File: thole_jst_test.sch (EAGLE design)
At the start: 3 parts, among them J1 Vertical Qwiic Connector

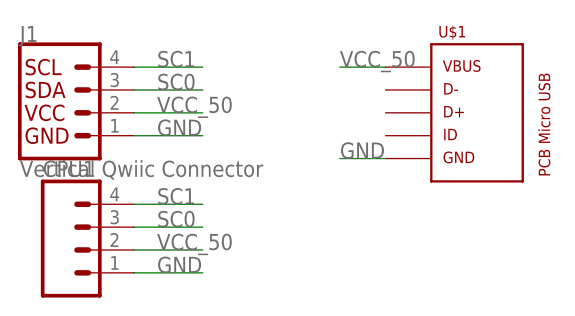
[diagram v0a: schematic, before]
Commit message: Goddamit jst throughole test wasn't throughhole
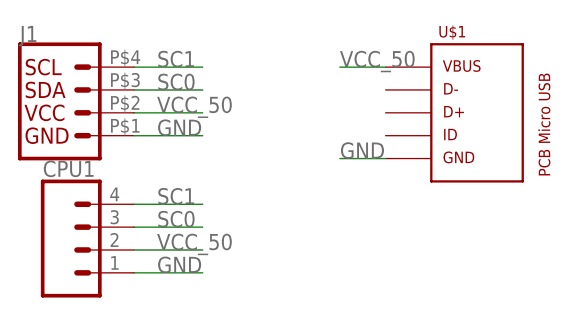
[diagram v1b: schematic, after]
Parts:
- J1: device SparkFun-Connectors:QWIIC_CONNECTOR -> 00jim:QWIIC_CONNECTORJST04_1MM_HOLE
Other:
- moved on the sheet: J1
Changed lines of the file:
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@@
 <grid distance="0.1" unitdist="inch" unit="inch" style="lines" multiple="1" display="no" altdistance="0.01" altunitdist="inch" altunit="inch"/>
 <layers>
-<layer number="1" name="Top" color="4" fill="1" visible="no" active="no"/>
-<layer number="16" name="Bottom" color="1" fill="1" visible="no" active="no"/>
-<layer number="17" name="Pads" color="2" fill="1" visible="no" active="no"/>
-<layer number="18" name="Vias" color="2" fill="1" visible="no" active="no"/>
-<layer number="19" name="Unrouted" color="6" fill="1" visible="no" active="no"/>
-<layer number="20" name="Dimension" color="24" fill="1" visible="no" active="no"/>
-<layer number="21" name="tPlace" color="7" fill="1" visible="no" active="no"/>
-<layer number="22" name="bPlace" color="7" fill="1" visible="no" active="no"/>
-<layer number="23" name="tOrigins" color="15" fill="1" visible="no" active="no"/>
-<layer number="24" name="bOrigins" color="15" fill="1" visible="no" active="no"/>
-<layer number="25" name="tNames" color="7" fill="1" visible="no" active="no"/>
-<layer number="26" name="bNames" color="7" fill="1" visible="no" active="no"/>
-<layer number="27" name="tValues" color="7" fill="1" visible="no" active="no"/>
-<layer number="28" name="bValues" color="7" fill="1" visible="no" active="no"/>
+<layer number="1" name="Top" color="4" fill="1" visible="yes" active="no"/>
+<layer number="16" name="Bottom" color="1" fill="1" visible="yes" active="no"/>
+<layer number="17" name="Pads" color="2" fill="1" visible="yes" active="no"/>
+<layer number="18" name="Vias" color="2" fill="1" visible="yes" active="no"/>
+<layer number="19" name="Unrouted" color="6" fill="1" visible="yes" active="no"/>
+<layer number="20" name="Dimension" color="24" fill="1" visible="yes" active="no"/>
+<layer number="21" name="tPlace" color="7" fill="1" visible="yes" active="no"/>
+<layer number="22" name="bPlace" color="7" fill="1" visible="yes" active="no"/>
+<layer number="23" name="tOrigins" color="15" fill="1" visible="yes" active="no"/>
+<layer number="24" name="bOrigins" color="15" fill="1" visible="yes" active="no"/>
+<layer number="25" name="tNames" color="7" fill="1" visible="yes" active="no"/>
+<layer number="26" name="bNames" color="7" fill="1" visible="yes" active="no"/>
+<layer number="27" name="tValues" color="7" fill="1" visible="yes" active="no"/>
+<layer number="28" name="bValues" color="7" fill="1" visible="yes" active="no"/>
 <layer number="29" name="tStop" color="7" fill="3" visible="no" active="no"/>
 <layer number="30" name="bStop" color="7" fill="6" visible="no" active="no"/>
@@
 <layer number="35" name="tGlue" color="7" fill="4" visible="no" active="no"/>
 <layer number="36" name="bGlue" color="7" fill="5" visible="no" active="no"/>
-<layer number="37" name="tTest" color="7" fill="1" visible="no" active="no"/>
-<layer number="38" name="bTest" color="7" fill="1" visible="no" active="no"/>
+<layer number="37" name="tTest" color="7" fill="1" visible="yes" active="no"/>
+<layer number="38" name="bTest" color="7" fill="1" visible="yes" active="no"/>
 <layer number="39" name="tKeepout" color="4" fill="11" visible="no" active="no"/>
 <layer number="40" name="bKeepout" color="1" fill="11" visible="no" active="no"/>
@@
 <layer number="44" name="Drills" color="7" fill="1" visible="no" active="no"/>
 <layer number="45" name="Holes" color="7" fill="1" visible="no" active="no"/>
-<layer number="46" name="Milling" color="3" fill="1" visible="no" active="no"/>
-<layer number="47" name="Measures" color="7" fill="1" visible="no" active="no"/>
-<layer number="48" name="Document" color="7" fill="1" visible="no" active="no"/>
-<layer number="49" name="Reference" color="7" fill="1" visible="no" active="no"/>
-<layer number="50" name="dxf" color="7" fill="1" visible="no" active="no"/>
-<layer number="51" name="tDocu" color="7" fill="1" visible="no" active="no"/>
-<layer number="52" name="bDocu" color="7" fill="1" visible="no" active="no"/>
-<layer number="53" name="tGND_GNDA" color="7" fill="9" visible="no" active="no"/>
-<layer number="54" name="bGND_GNDA" color="1" fill="9" visible="no" active="no"/>
-<layer number="56" name="wert" color="7" fill="1" visible="no" active="no"/>
-<layer number="57" name="tCAD" color="7" fill="1" visible="no" active="no"/>
-<layer number="59" name="tCarbon" color="7" fill="1" visible="no" active="no"/>
-<layer number="60" name="bCarbon" color="7" fill="1" visible="no" active="no"/>
+<layer number="46" name="Milling" color="3" fill="1" visible="yes" active="no"/>
+<layer number="47" name="Measures" color="7" fill="1" visible="yes" active="no"/>
+<layer number="48" name="Document" color="7" fill="1" visible="yes" active="no"/>
+<layer number="49" name="Reference" color="7" fill="1" visible="yes" active="no"/>
+<layer number="50" name="dxf" color="7" fill="1" visible="yes" active="no"/>
+<layer number="51" name="tDocu" color="7" fill="1" visible="yes" active="no"/>
+<layer number="52" name="bDocu" color="7" fill="1" visible="yes" active="no"/>
+<layer number="53" name="tGND_GNDA" color="7" fill="9" visible="yes" active="no"/>
+<layer number="54" name="bGND_GNDA" color="1" fill="9" visible="yes" active="no"/>
+<layer number="56" name="wert" color="7" fill="1" visible="yes" active="no"/>
+<layer number="57" name="tCAD" color="7" fill="1" visible="yes" active="no"/>
+<layer number="59" name="tCarbon" color="7" fill="1" visible="yes" active="no"/>
+<layer number="60" name="bCarbon" color="7" fill="1" visible="yes" active="no"/>
 <layer number="88" name="SimResults" color="9" fill="1" visible="yes" active="yes"/>
 <layer number="89" name="SimProbes" color="9" fill="1" visible="yes" active="yes"/>
@@
 <parts>
 <part name="CPU1" library="SparkFun-Connectors" deviceset="CONN_04" device="1X04_NO_SILK"/>
-<part name="J1" library="SparkFun-Connectors" deviceset="QWIIC_CONNECTOR" device="" value="Vertical Qwiic Connector"/>
+<part name="J1" library="00jim" deviceset="QWIIC_CONNECTOR" device="JST04_1MM_HOLE" value="Vertical Qwiic Connector"/>
 <part name="U$1" library="USB_pcb_connectors" deviceset="PCB_MICRO_USB_B" device="SS_2"/>
 </parts>
@@
 </instance>
 <instance part="J1" gate="G$1" x="17.78" y="33.02" smashed="yes">
-<attribute name="VALUE" x="12.7" y="27.686" size="1.778" layer="96" font="vector" align="top-left"/>
 <attribute name="NAME" x="12.7" y="40.894" size="1.778" layer="95" font="vector"/>
 </instance>
